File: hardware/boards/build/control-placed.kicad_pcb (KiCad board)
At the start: 4 copper layers, 177.9 x 107.5 mm, 108 parts

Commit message: Refactor hardware pipeline: config-driven scripts, immutable build stages, full 3D export
- Reorganize scripts/ into build/, common/, placement/, routing/, export/, models/
- Replace autoroute.sh (389 lines bash) with autoroute.py (pure Python)
- Extract board-specific values into board-config.json (placement, routing, DRC allowlist)
- Create hardware/Makefile with file-based dependencies covering full pipeline
- Immutable pipeline: placed → routed → poured → 3d → step → glb (no in-place mutation)
- Ground pours now read clearances from design-rules.json
- DRC allowlisting for known SD card footprint errors
- 3D pipeline: add_3d_models → export_3d_assembly (STEP) → export_gltf (GLB with named nodes)
- Simplify root Makefile to delegate hw-* targets to hardware/Makefile
- Remove Docker/CI workflows (unused), old flat scripts, pycache
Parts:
- removed R11: 100000Ω, UNI_ROYAL_0402WGF1003TCE:R0402
- removed R12: 10000Ω, UNI_ROYAL_0603WAF1002T5E:R0603
- removed the REF** at (84.7, 11.9)
- removed the REF** at (75.0, 35.1)
- added R8: 100Ω, UNI_ROYAL_0603WAF1000T5E:R0603, F.Cu at (68.2, 45.8)
- added R9: 100000Ω, UNI_ROYAL_0402WGF1003TCE:R0402, F.Cu at (68.3, 39.0)
- added REF**: HTSSOP-32, TLC5947DAP:HTSSOP-32, F.Cu at (84.7, 11.9)
- added REF**: HTSSOP-32, TLC5947DAP:HTSSOP-32, B.Cu at (75.0, 35.1)
- C12, C7: moved to B.Cu
- C13, C6: moved to F.Cu
- R10: value 100Ω -> 10000Ω; footprint UNI_ROYAL_0603WAF1000T5E:R0603 -> UNI_ROYAL_0603WAF1002T5E:R0603; moved to B.Cu
- moved C10 33.7 mm to (78.1, 46.8)
- moved C8 32.3 mm to (103.6, 60.8)
- moved C12 22.9 mm to (81.5, 67.1), turned to 180 degrees
- moved C9 22.9 mm to (103.6, 60.8)
- moved C11 21.3 mm to (78.3, 40.8)
- moved R10 19.7 mm to (78.1, 62.8), turned to 180 degrees
- moved C6 15.7 mm to (78.0, 62.1), turned to 0 degrees
- moved C13 5.15 mm to (106.3, 65.2), turned to 0 degrees
- moved C7 0.42 mm to (78.3, 46.4), turned to 180 degrees
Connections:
- C11 pad 1: c_lcd_rst-power-hv -> c_sd-power-hv
- C8 pad 1: c_sd-power-hv -> c_lcd_rst-power-hv
- R10 pad 1: lcd_bl -> c_sd-power-hv
- R10 pad 2: gate -> c_lcd_rst-power-hv

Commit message: Multi algo
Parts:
- removed the REF** at (129.0, 36.5)
- removed the REF** at (129.0, 49.3)
- removed the REF** at (143.0, 49.3)
- removed the REF** at (157.0, 22.5)
- removed the REF** at (129.0, 100.5)
- removed the REF** at (129.0, 74.9)
- removed the REF** at (84.7, 11.9)
- removed the REF** at (143.0, 74.9)
- removed the REF** at (157.0, 62.1)
- removed the REF** at (143.0, 36.5)
- removed the REF** at (129.0, 62.1)
- removed the REF** at (171.0, 36.5)
- removed the REF** at (143.0, 100.5)
- removed the REF** at (157.0, 87.7)
- removed the REF** at (171.0, 49.3)
- removed the REF** at (157.0, 49.3)
- removed the REF** at (31.9, 31.5)
- removed the REF** at (171.0, 100.5)
- removed the REF** at (171.0, 87.7)
- removed the REF** at (171.0, 74.9)
- removed the REF** at (143.0, 87.7)
- removed the REF** at (171.0, 62.1)
- removed the REF** at (22.3, 5.50)
- removed the REF** at (157.0, 74.9)
- removed the REF** at (143.0, 62.1)
- removed the REF** at (157.0, 100.5)
- removed the REF** at (129.0, 87.7)
- removed the REF** at (75.0, 35.1)
- removed the REF** at (76.0, 1.50)
- removed the REF** at (30.0, 1.50)
- removed the REF** at (35.5, 1.50)
- removed the REF** at (59.2, 27.6)
- removed the REF** at (22.0, 5.50)
- removed the REF** at (48.8, 27.6)
- removed the REF** at (171.0, 22.5)
- removed the REF** at (41.0, 1.50)
- removed the REF** at (70.5, 1.50)
- removed the REF** at (157.0, 36.5)
- added REF**: PJ398SM, PJ398SM:PJ398SM, F.Cu at (139.9, 63.7)
- added REF**: HTSSOP-32, TLC5947DAP:HTSSOP-32, F.Cu at (58.1, 62.7)
- added REF**: PJ398SM, PJ398SM:PJ398SM, F.Cu at (161.9, 17.5)
- added REF**: PJ398SM, PJ398SM:PJ398SM, F.Cu at (161.9, 79.1)
- added REF**: PJ398SM, PJ398SM:PJ398SM, F.Cu at (139.9, 32.9)
- added REF**: PJ398SM, PJ398SM:PJ398SM, F.Cu at (172.9, 48.3)
- added REF**: PJ398SM, PJ398SM:PJ398SM, F.Cu at (150.9, 94.5)
- added REF**: PJ398SM, PJ398SM:PJ398SM, F.Cu at (139.9, 79.1)
- added REF**: SOIC-16, 74HC165D:SOIC-16, F.Cu at (70.5, 45.0)
- added REF**: PJ398SM, PJ398SM:PJ398SM, F.Cu at (161.9, 94.5)
- added REF**: PJ398SM, PJ398SM:PJ398SM, F.Cu at (161.9, 32.9)
- added REF**: SIP-9, ResistorNetwork9:SIP-9, F.Cu at (48.2, 25.5)
- added REF**: PJ398SM, PJ398SM:PJ398SM, F.Cu at (139.9, 94.5)
- added REF**: PJ398SM, PJ398SM:PJ398SM, F.Cu at (150.9, 63.7)
- added REF**: PJ398SM, PJ398SM:PJ398SM, F.Cu at (172.9, 79.1)
- added REF**: PJ398SM, PJ398SM:PJ398SM, F.Cu at (172.9, 17.5)
- added REF**: SOIC-16, 74HC165D:SOIC-16, F.Cu at (49.3, 63.2)
- added REF**: PJ398SM, PJ398SM:PJ398SM, F.Cu at (139.9, 17.5)
- added REF**: SIP-9, ResistorNetwork9:SIP-9, F.Cu at (95.8, 33.2)
- added REF**: SIP-9, ResistorNetwork9:SIP-9, F.Cu at (29.8, 64.9)
- added REF**: PJ398SM, PJ398SM:PJ398SM, F.Cu at (150.9, 32.9)
- added REF**: PJ398SM, PJ398SM:PJ398SM, F.Cu at (150.9, 79.1)
- added REF**: PJ398SM, PJ398SM:PJ398SM, F.Cu at (150.9, 48.3)
- added REF**: SIP-9, ResistorNetwork9:SIP-9, F.Cu at (75.3, 64.8)
- added REF**: PJ398SM, PJ398SM:PJ398SM, F.Cu at (161.9, 63.7)
- added REF**: PJ398SM, PJ398SM:PJ398SM, F.Cu at (172.9, 32.9)
- added REF**: PJ398SM, PJ398SM:PJ398SM, F.Cu at (161.9, 48.3)
- added REF**: PJ398SM, PJ398SM:PJ398SM, F.Cu at (150.9, 17.5)
- added REF**: PJ398SM, PJ398SM:PJ398SM, F.Cu at (172.9, 94.5)
- added REF**: HTSSOP-32, TLC5947DAP:HTSSOP-32, F.Cu at (35.6, 56.9)
- added REF**: SOIC-16, 74HC165D:SOIC-16, F.Cu at (61.8, 45.5)
- added REF**: PJ398SM, PJ398SM:PJ398SM, F.Cu at (139.9, 48.3)
- added REF**: SIP-9, ResistorNetwork9:SIP-9, F.Cu at (42.4, 46.8)
- added REF**: PJ366ST, PJ366ST:PJ366ST, F.Cu at (128.9, 101.0)
- added REF**: PJ366ST, PJ366ST:PJ366ST, F.Cu at (128.9, 85.6)
- added REF**: SOIC-16, 74HC165D:SOIC-16, B.Cu at (56.5, 63.6)
- added REF**: SOIC-16, 74HC165D:SOIC-16, B.Cu at (48.2, 54.2)
- added REF**: PJ398SM, PJ398SM:PJ398SM, F.Cu at (172.9, 63.7)
- C13, C4, C6, C8, R1, R2, R8: moved to B.Cu
- C2, C7, R10, R3, R5, R6, R7, REF**: moved to F.Cu
- moved R7 69.6 mm to (44.1, 36.5), turned to 0 degrees
- moved R2 65.0 mm to (62.6, 62.7), turned to 180 degrees
- moved C5 53.2 mm to (58.9, 24.7)
- moved C6 50.7 mm to (128.7, 59.6), turned to 180 degrees
- moved C3 49.7 mm to (37.5, 28.5)
- moved R10 48.0 mm to (126.0, 59.6), turned to 0 degrees
- moved R1 47.2 mm to (35.9, 56.8), turned to 180 degrees
- moved C11 45.0 mm to (66.1, 84.1)
- moved C8 44.7 mm to (67.5, 34.4), turned to 180 degrees
- moved C9 42.0 mm to (67.2, 39.8)
- moved R5 38.9 mm to (121.4, 101.0), turned to 0 degrees
- moved C10 37.8 mm to (64.1, 81.9)
- moved C2 36.5 mm to (119.7, 31.6), turned to 0 degrees
- moved R9 36.2 mm to (95.5, 63.0)
- moved R3 35.9 mm to (55.0, 21.0), turned to 0 degrees
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
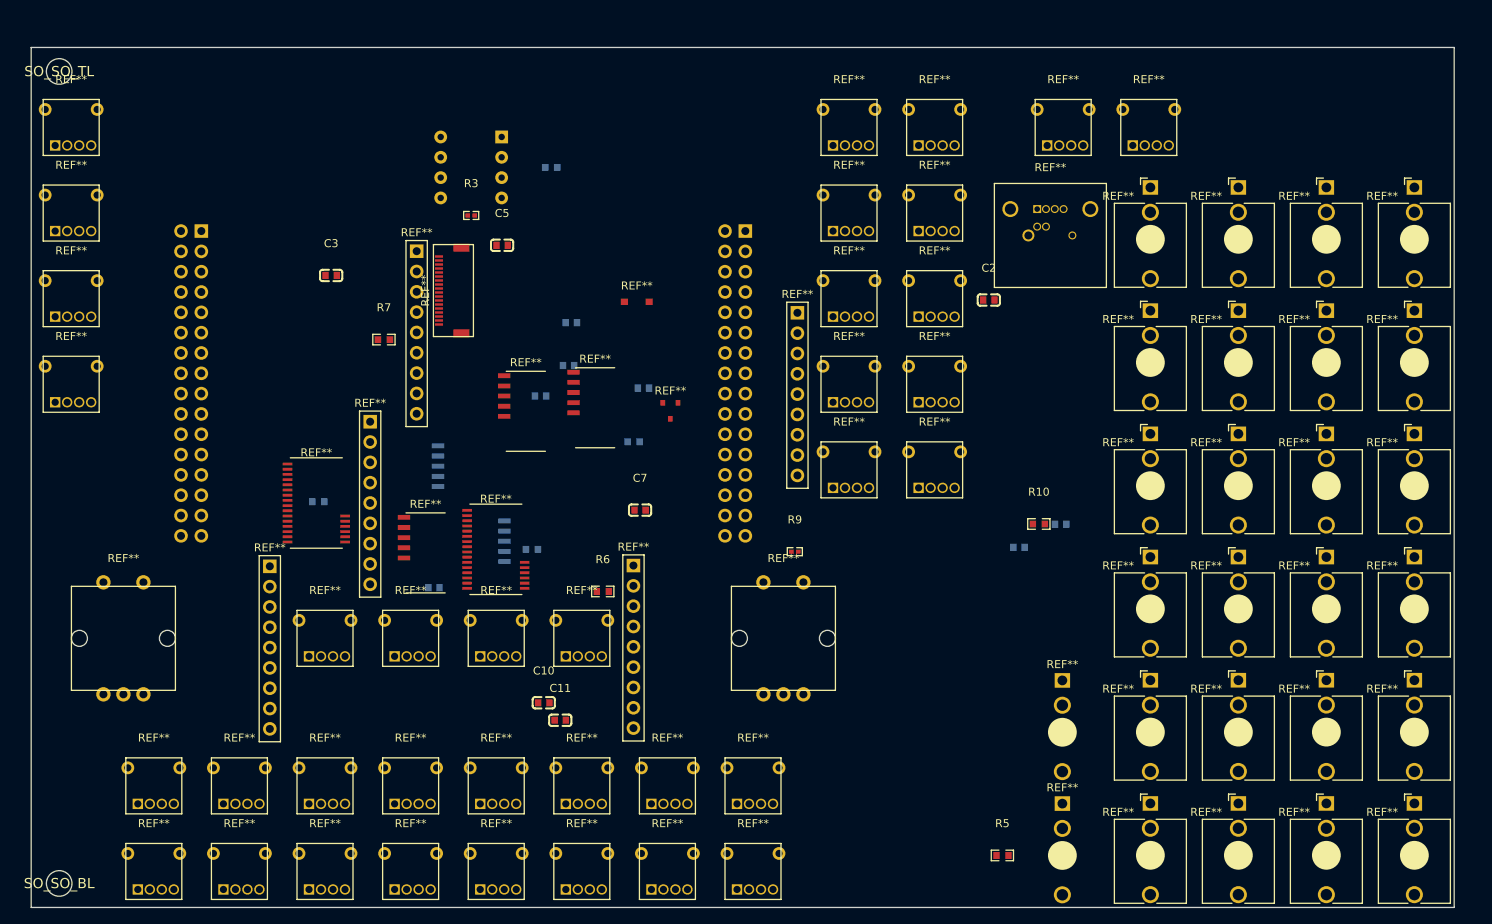
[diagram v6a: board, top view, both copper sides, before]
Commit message: Multi algo parts placement and functioning gerber export
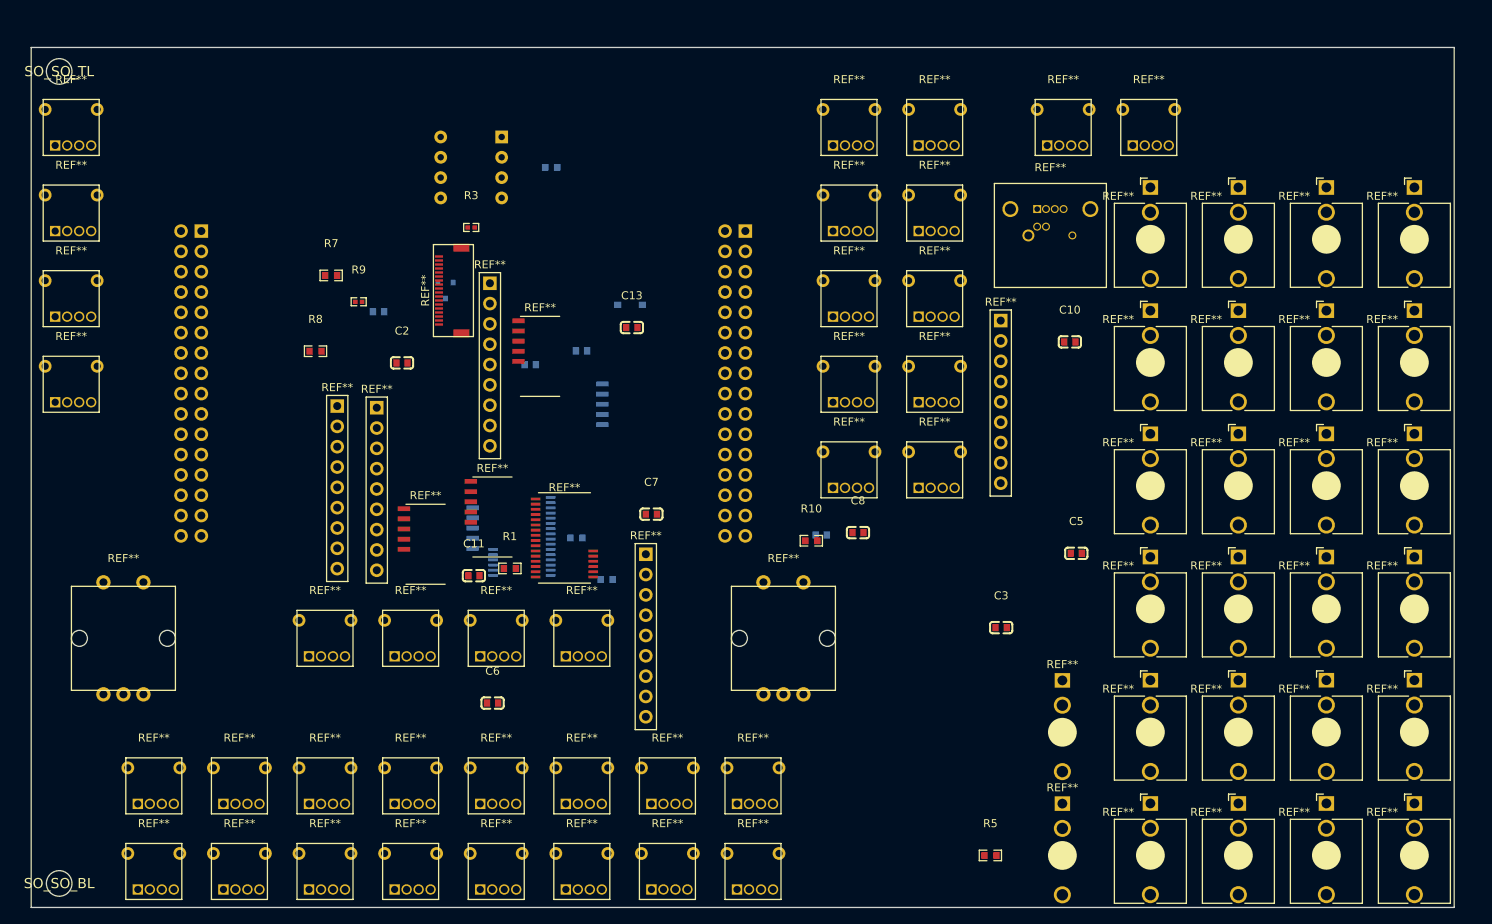
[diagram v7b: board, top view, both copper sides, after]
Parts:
- C13, C6, C8, R1, R8, REF** (x2): moved to F.Cu
- R6, REF** (x5): moved to B.Cu
- moved C3 94.6 mm to (121.3, 72.5)
- moved C5 81.5 mm to (130.6, 63.2)
- moved C10 79.7 mm to (129.8, 36.8)
- moved C6 74.4 mm to (57.7, 82.0), turned to 0 degrees
- moved C2 73.8 mm to (46.4, 39.4)
- moved R9 62.8 mm to (40.9, 31.8)
- moved C13 55.6 mm to (75.1, 35.0), turned to 0 degrees
- moved REF** 47.0 mm to (76.8, 63.3)
- moved C8 44.4 mm to (103.4, 60.6), turned to 0 degrees
- moved R8 41.3 mm to (35.5, 38.0), turned to 0 degrees
- moved C9 38.0 mm to (98.8, 60.9)
- moved REF** 37.7 mm to (43.2, 45.0)
- moved REF** 31.9 mm to (51.8, 30.4), turned to 180 degrees
- moved C1 30.4 mm to (62.4, 39.7)
- moved R10 28.5 mm to (97.5, 61.7)
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
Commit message: Single sided SMD assebly
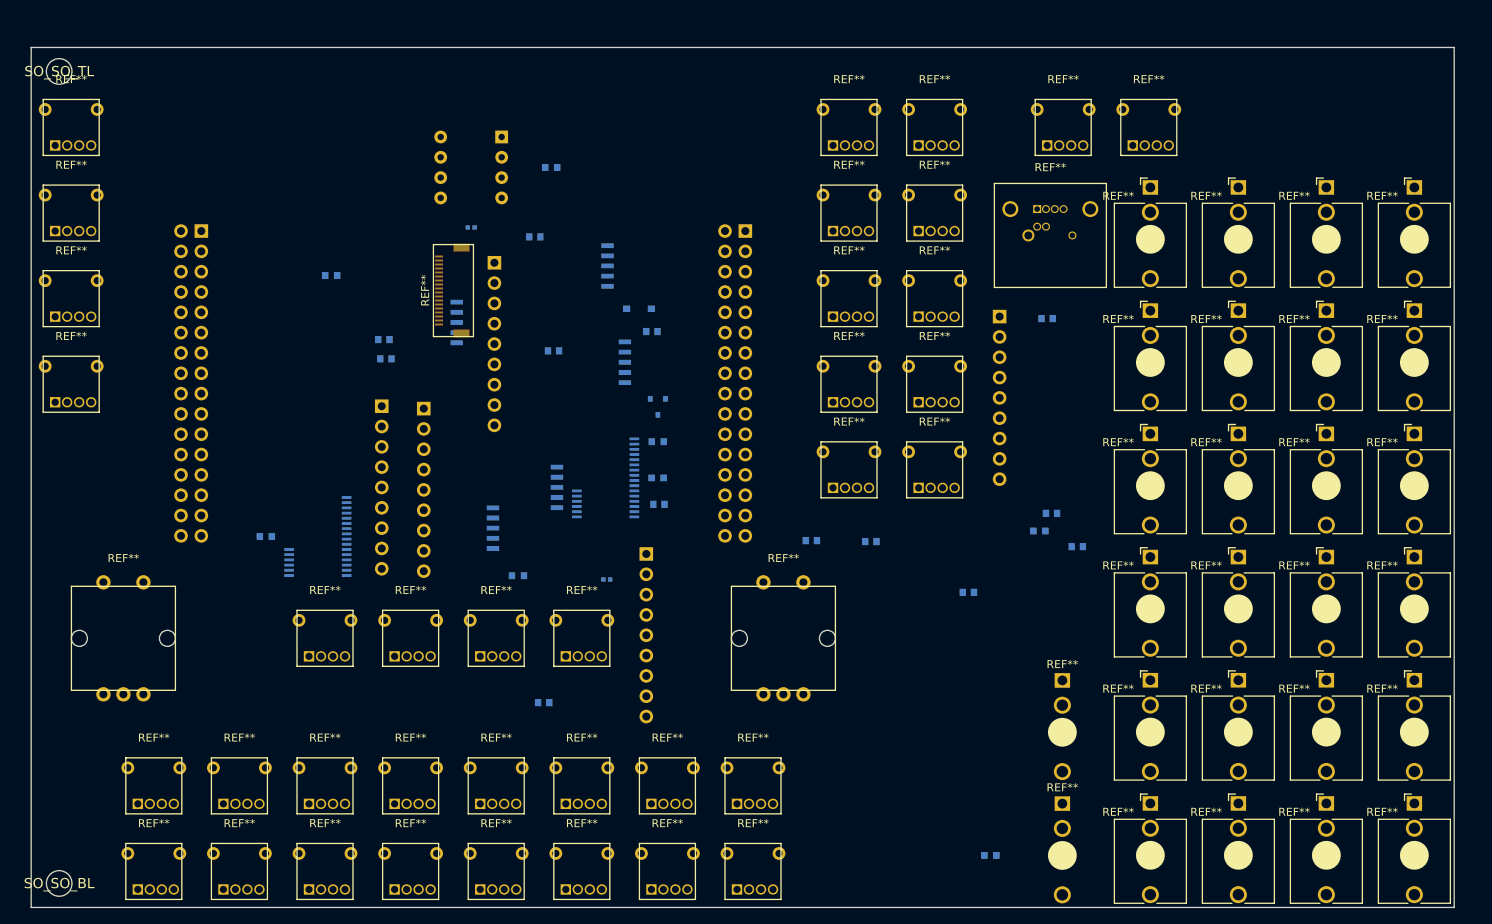
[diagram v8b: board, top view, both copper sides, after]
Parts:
- C10, C11, C13, C2, C3, C5, C6, C7, C8, R1, R10, R3, R5, R7, R8, R9, REF** (x9): moved to B.Cu
- moved C12 87.8 mm to (127.5, 58.2)
- moved C3 85.1 mm to (44.1, 36.5), turned to 180 degrees
- moved C2 80.8 mm to (127.0, 33.9), turned to 180 degrees
- moved C6 75.7 mm to (130.8, 62.4), turned to 180 degrees
- moved C11 61.8 mm to (117.1, 68.1), turned to 180 degrees
- moved C8 54.8 mm to (63.0, 23.7), turned to 180 degrees
- moved C10 52.3 mm to (77.6, 35.5), turned to 180 degrees
- moved C13 48.2 mm to (64.1, 81.9), turned to 180 degrees
- moved R9 46.5 mm to (72.0, 66.5), turned to 180 degrees
- moved R8 44.2 mm to (78.3, 49.3), turned to 180 degrees
- moved C5 33.2 mm to (97.5, 61.7), turned to 180 degrees
- moved R1 30.8 mm to (29.3, 61.1), turned to 180 degrees
- moved REF** 30.3 mm to (78.3, 44.9)
- moved R10 28.5 mm to (126.0, 60.4), turned to 180 degrees
- moved C7 27.7 mm to (105.0, 61.8), turned to 180 degrees
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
